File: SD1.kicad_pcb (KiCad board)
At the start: 4 copper layers, 296.7 x 122.7 mm, 246 parts, among them J101 HR861153C, J102 10118194-0001LF, J103 JST ZH 1.5mm 1x5, J104 JST 1.25mm, J107 JST 1.25mm, J301 PJ-102AH, J302 PJ-102AH, J303 Conn_01x02, J304 Conn_01x02, J402 Conn_ARM_JTAG_SWD_10, J403 FTDI_TTL_Cable, J801 Conn_01x02, J802 Conn_01x02, Q1 FDT86244, Q101 BSS138, Q102 PDTC114EU,115, Q301 DMMT5401, Q302 DMMT5401, Q801 DMMT5401, Q802 DMMT5401, SW103 Multidirection_Switch, SW401 PTS810, T1 HR051067, U102 ER-TFTM028-4, U103 CP2102N-A02-GQFN28R, U104 CC2652P, U105 W5500, U106 EKMC1691111, U107 MCP23017, U108 BME280, U109 SCD30, U2 TPS23753A, U3 TL431A, U301 110-102, U302 LMP91000, U4 TCMT1107, U501 TLV70018, U502 ADPD188BI, U503 Smoke Chamber, U601 CCS811, U701 TPS61022, U702 TLV62585, U801 MCP73831-2-OT, Y101 25MHz

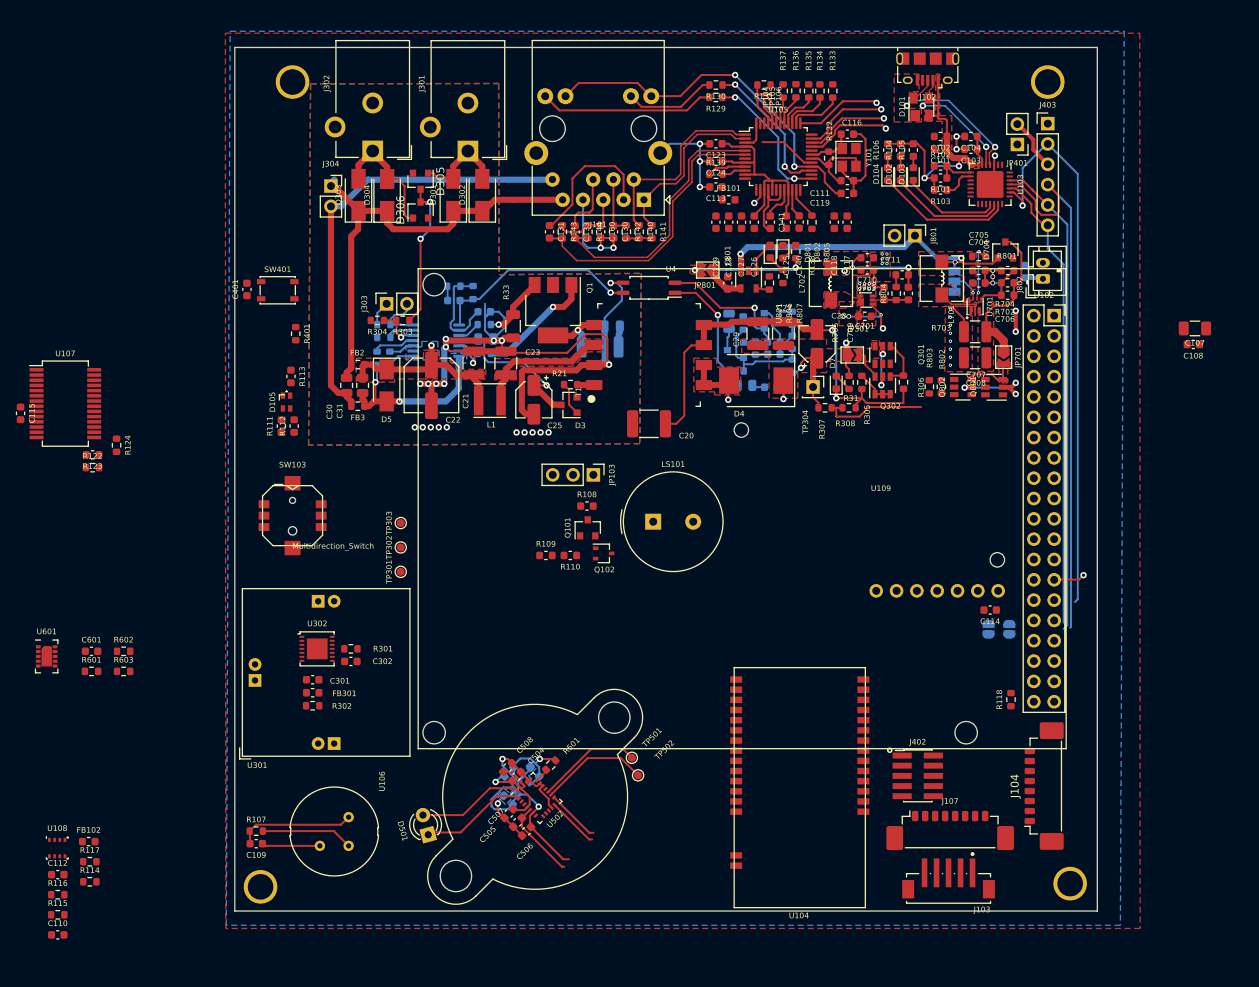
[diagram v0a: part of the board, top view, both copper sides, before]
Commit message: 4layer layout WIP, 90%.
Changed SCD30 to reverse mount. 
Connected RGB led and button to io expander.
Connected all nets to micro.
Add jumper for CTS line.
Nettie GNDA and GND for W5500 Eth.
Changed EN_5V_BST to Global.
Bugfixes net names: LCD_CS
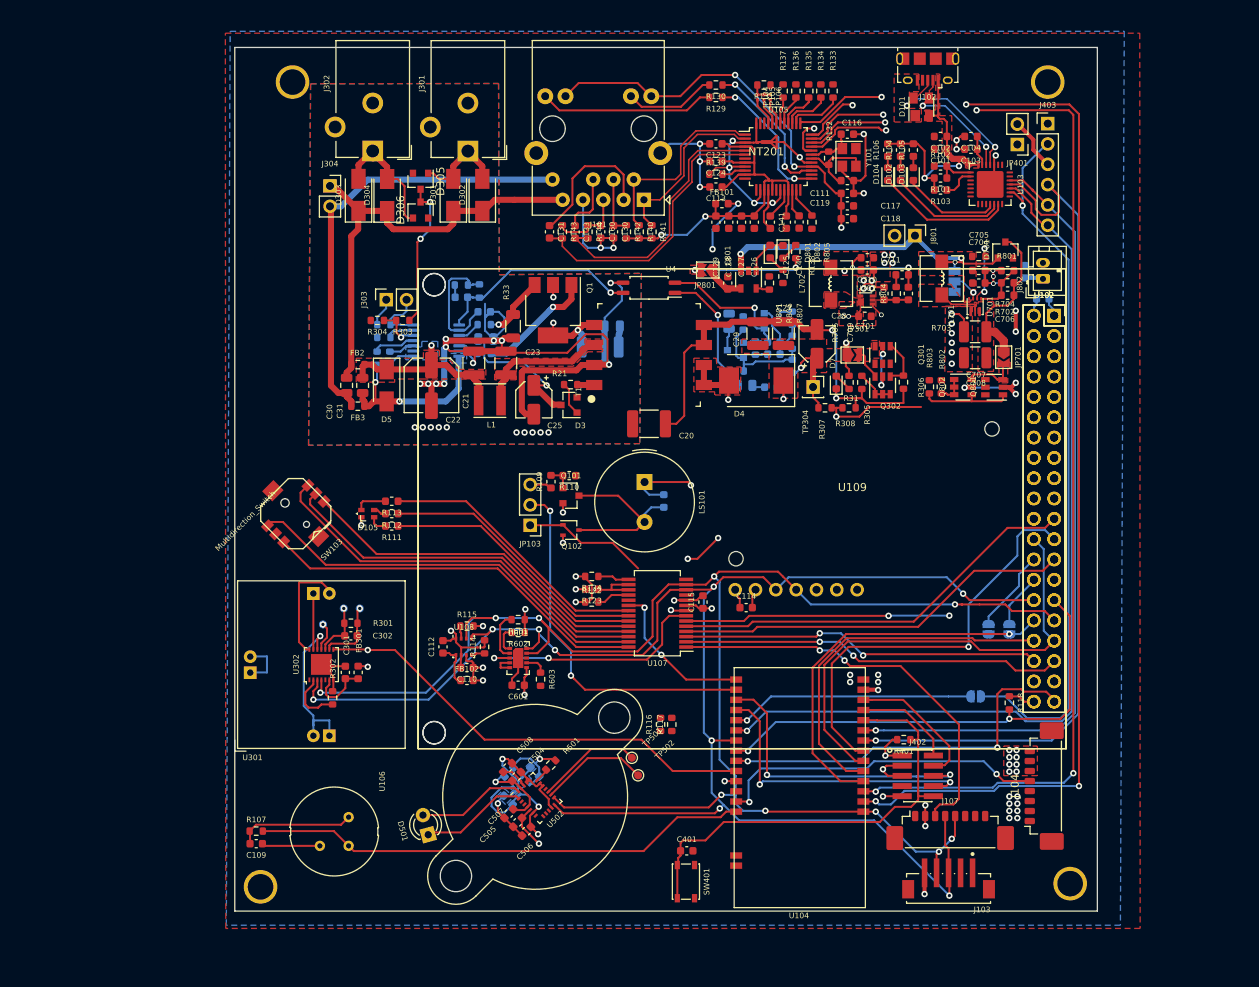
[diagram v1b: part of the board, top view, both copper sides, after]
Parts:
- removed C107: 10u, Capacitor_SMD:C_1206_3216Metric
- added JP107: Jumper_NO_Small, Jumper:SolderJumper-2_P1.3mm_Open_RoundedPad1.0x1.5mm, B.Cu at (208.2, 87.6)
- added NT201: Net-Tie_2, NetTie:NetTie-2_SMD_Pad0.5mm, F.Cu at (182.0, 18.3)
- added U102: ER-TFTM028-4, mylib:ER-TFTM028-4, F.Cu at (218.0, 40.0)
- C108, R108, TP301, TP302, TP303: moved to B.Cu
- U109: footprint mylib:SCD30 -> mylib:SCD30_reverse_mount
- moved R401 91.4 mm to (199.2, 93.0), turned to 180 degrees
- moved SW401 89.8 mm to (172.0, 110.7), turned to 270 degrees
- moved C401 89.1 mm to (172.1, 106.9), turned to 0 degrees
- moved C115 88.5 mm to (174.1, 75.8), turned to 90 degrees
- moved U107 78.5 mm to (168.4, 77.2), turned to 180 degrees
- moved R116 78.3 mm to (168.8, 91.1), turned to 90 degrees
- moved R117 74.7 mm to (170.2, 91.1), turned to 90 degrees
- moved R122 64.6 mm to (160.2, 75.8)
- moved R123 64.6 mm to (160.2, 74.2)
- moved R115 62.6 mm to (144.6, 78.8)
- moved R124 61.6 mm to (160.2, 72.6), turned to 180 degrees
- moved C110 61.1 mm to (144.6, 84.0), turned to 180 degrees
- moved U601 58.9 mm to (151.0, 82.8)
- moved R114 57.4 mm to (146.8, 81.4), turned to 90 degrees
- moved U108 56.7 mm to (144.2, 81.4)
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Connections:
- J104 pad 5: (no net) -> /RGBW_DOUT
- J402 pad 1: /TARGET_VDD -> +3V3
- J403 pad 6: /Debug and Serial/WMCU_CTS -> /WMCU_CTS
- JP103 pad 2: (no net) -> /SPKR_DRIVE
- R401 pad 2: /TARGET_VDD -> +3V3
- R801 pad 1: /Power/EN_5V_BST -> EN_5V_BST
- U102 pad 21: (no net) -> /~LCD_RESET
- U102 pad 23: (no net) -> /~LCD_CS
- U102 pad 39: (no net) -> /CTP_INT
- U103 pad 24: /Debug and Serial/WMCU_CTS -> /WMCU_CTS
- U104 pad 15: (no net) -> /IO_INT
- U104 pad 16: (no net) -> /SPKR_DRIVE
- U104 pad 2: (no net) -> /~ETH_INT
- U104 pad 20: (no net) -> /WMCU_CTS
- U104 pad 22: (no net) -> /LCD_BACKLIGHT
- U104 pad 23: (no net) -> /CTP_INT
- U104 pad 27: (no net) -> /RGBW_DOUT
- U104 pad 28: (no net) -> /PIR_SENSE
- U104 pad 3: (no net) -> /ETH_CS
- U104 pad 7: (no net) -> /~LCD_CS
- U105 pad 32: (no net) -> /ETH_CS
- U105 pad 36: (no net) -> /~ETH_INT
- U107 pad 1: /SD_CS -> /EXT_Sleep
- U107 pad 2: (no net) -> /SD_CS
- U107 pad 20: (no net) -> /IO_INT
- U107 pad 21: /I_LED_R -> /I_LED_B
- U107 pad 23: /I_LED_B -> /I_LED_R
- U107 pad 3: /LCD_DC -> /FONT_CS
- U107 pad 4: /FONT_CS -> /LCD_DC
- U107 pad 5: (no net) -> /~LCD_RESET
- U107 pad 8: /EXT_Sleep -> EN_5V_BST
- U701 pad 5: /Power/EN_5V_BST -> EN_5V_BST
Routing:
- net +3V3: track 112.9 -> 441.0 mm, vias 6 -> 23
- net I2C_SDA: track 6.78 -> 212.5 mm, vias 0 -> 10
- net I2C_SCL: track 6.49 -> 211.7 mm, vias 0 -> 9
- net +5V: track 68.0 -> 218.8 mm, vias 11 -> 20
- net /~ETH_INT: track 0.00 -> 148.9 mm, vias 0 -> 4
- net /ETH_CS: track 0.00 -> 148.7 mm, vias 0 -> 4
- net /WMCU_CTS: track 0.00 -> 113.3 mm, vias 0 -> 1
- net EN_5V_BST: track 0.00 -> 94.7 mm, vias 0 -> 3
- net 5V_MainDet: track 13.6 -> 79.0 mm, vias 0 -> 4
- net /LCD_BACKLIGHT: track 0.00 -> 59.6 mm, vias 0 -> 2
- net SPI_SCK: track 91.1 -> 150.1 mm
- net /WMCU_RESET: track 0.00 -> 58.6 mm
- net /Debug and Serial/WMCU_CTS: track 57.8 -> 0.00 mm
- net /CO_ADC: track 0.00 -> 56.6 mm, vias 0 -> 1
- net SPI_MOSI: track 98.7 -> 153.1 mm, vias 2 -> 1
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- added copper zone on F.Cu, net +5V
- added copper zone on F.Cu, net /Debug and Serial/5V_USB
- added copper zone on In2.Cu, net GND
- removed copper zone on F.Cu, net /5V_USB
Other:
- net class Default: clearance 0.2 -> 0.1524
- rule trace_clearance: 0.2 -> 0.1524

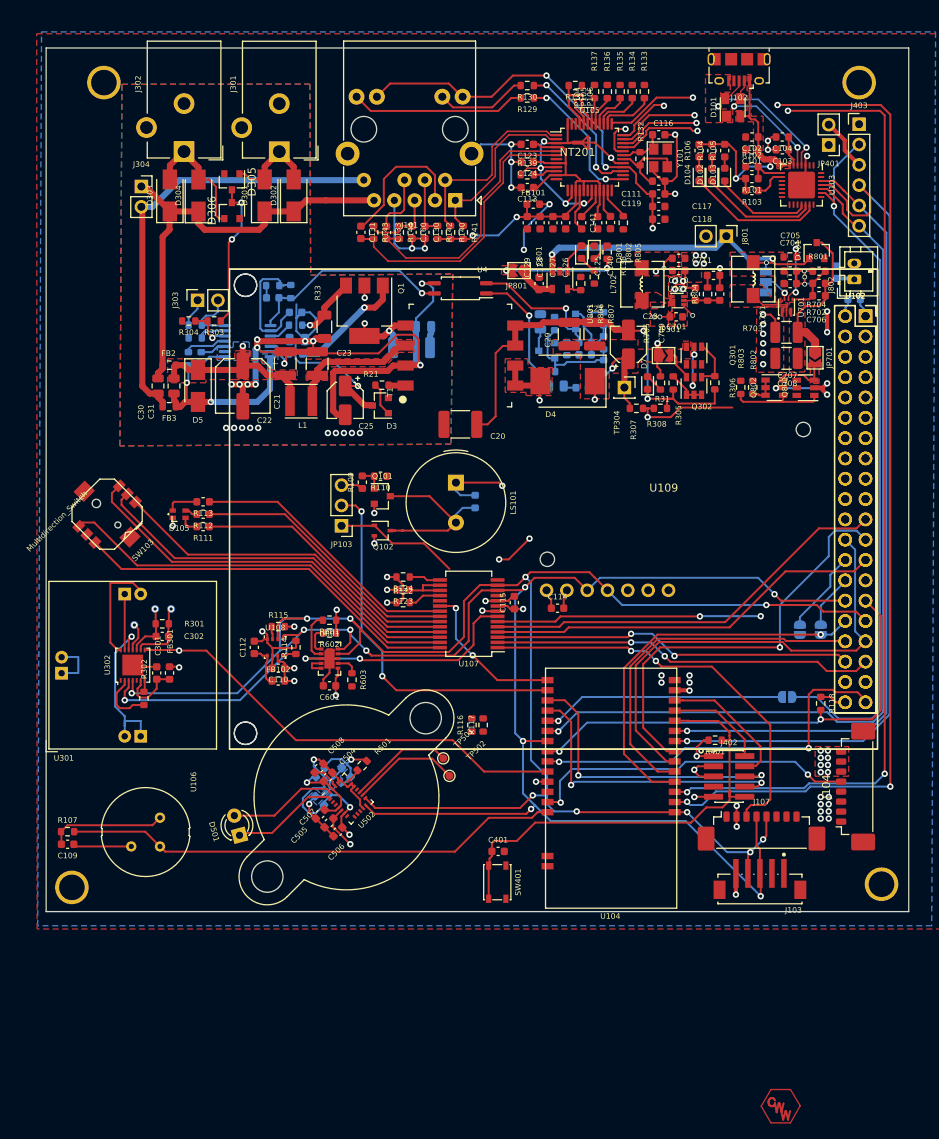
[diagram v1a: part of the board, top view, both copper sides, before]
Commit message: Layout WIP, sch final
USB 5V Jumper works for both FTDI and microusb
Added decoupling caps for micro
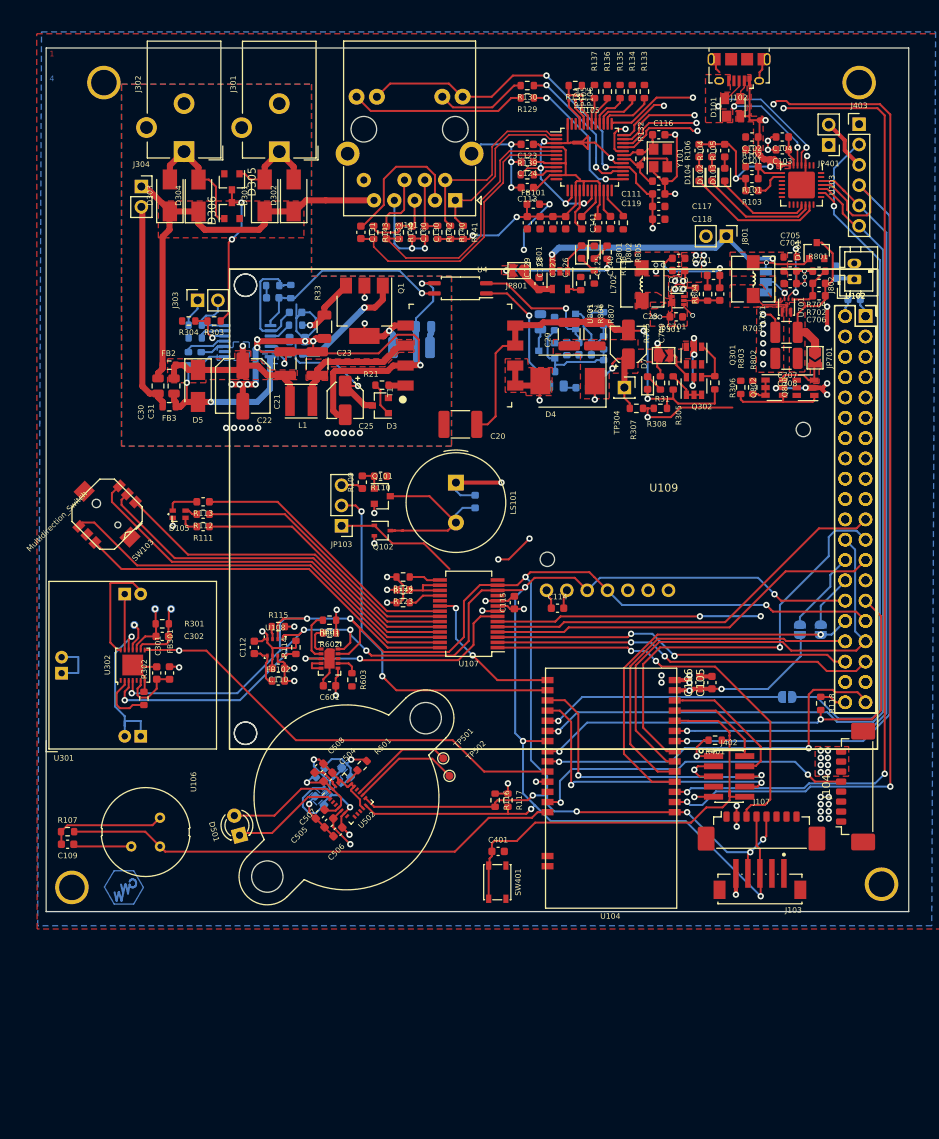
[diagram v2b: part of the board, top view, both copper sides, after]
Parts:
- added C105: 10u, Capacitor_SMD:C_0603_1608Metric, F.Cu at (198.8, 85.8)
- added C106: 1u, Capacitor_SMD:C_0603_1608Metric, F.Cu at (197.3, 85.8)
- LOGO101: moved to B.Cu
- moved LOGO101 86.5 mm to (125.3, 111.5), turned to 180 degrees
- moved R117 9.90 mm to (173.3, 100.5), turned to 270 degrees
- moved R116 9.84 mm to (171.7, 100.5), turned to 270 degrees
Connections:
- J403 pad 3: Net-(J403-Pad3) -> /Debug and Serial/5V_USB
- JP401 pad 2: Net-(J403-Pad3) -> /Debug and Serial/5V_USB
- U102 pad 10: (no net) -> Net-(U102-Pad10) (x2)
- U102 pad 11: (no net) -> Net-(U102-Pad11) (x2)
- U102 pad 12: (no net) -> Net-(U102-Pad12) (x2)
- U102 pad 13: (no net) -> Net-(U102-Pad13) (x2)
- U102 pad 14: (no net) -> Net-(U102-Pad14) (x2)
- U102 pad 15: (no net) -> Net-(U102-Pad15) (x2)
- U102 pad 16: (no net) -> Net-(U102-Pad16) (x2)
- U102 pad 17: (no net) -> Net-(U102-Pad17) (x2)
- U102 pad 18: (no net) -> Net-(U102-Pad18) (x2)
- U102 pad 19: (no net) -> Net-(U102-Pad19) (x2)
- U102 pad 20: (no net) -> Net-(U102-Pad20) (x2)
- U102 pad 22: (no net) -> Net-(U102-Pad22) (x2)
- U102 pad 3: (no net) -> Net-(U102-Pad3) (x2)
- U102 pad 37: (no net) -> Net-(U102-Pad37) (x2)
- U102 pad 38: (no net) -> Net-(U102-Pad38) (x2)
- U102 pad 4: (no net) -> Net-(U102-Pad4) (x2)
- U102 pad 5: (no net) -> Net-(U102-Pad5) (x2)
- U102 pad 6: (no net) -> Net-(U102-Pad6) (x2)
- U102 pad 7: (no net) -> Net-(U102-Pad7) (x2)
- U102 pad 8: (no net) -> Net-(U102-Pad8) (x2)
- U102 pad 9: (no net) -> Net-(U102-Pad9) (x2)
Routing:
- net +5V: track 218.8 -> 277.3 mm, vias 20 -> 22
- net +3V3: track 441.0 -> 470.1 mm, vias 23 -> 26
- net /Debug and Serial/5V_USB: track 32.0 -> 48.4 mm, vias 2 -> 3
- net GND: track 216.0 -> 225.7 mm
- net Net-(J403-Pad3): track 6.65 -> 0.00 mm
- net 5V_Main: track 58.8 -> 57.8 mm
- net I2C_SCL: track 211.7 -> 212.6 mm
- net 5V_MainDet: track 79.0 -> 78.5 mm
- added copper zone on In1.Cu, net +3V3
- added copper zone on F.Cu, net /Eth + PoE/PoE Flyback/VP
- added copper zone on In1.Cu, net GNDD
- removed copper zone on F.Cu, net (none)
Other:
- board text added: "1"
- board text added: "2"
- board text added: "3"
- board text added: "4"
- board text added: "SAEMS r0, 12/12/20 Daniel Mulvaney Clayton White"

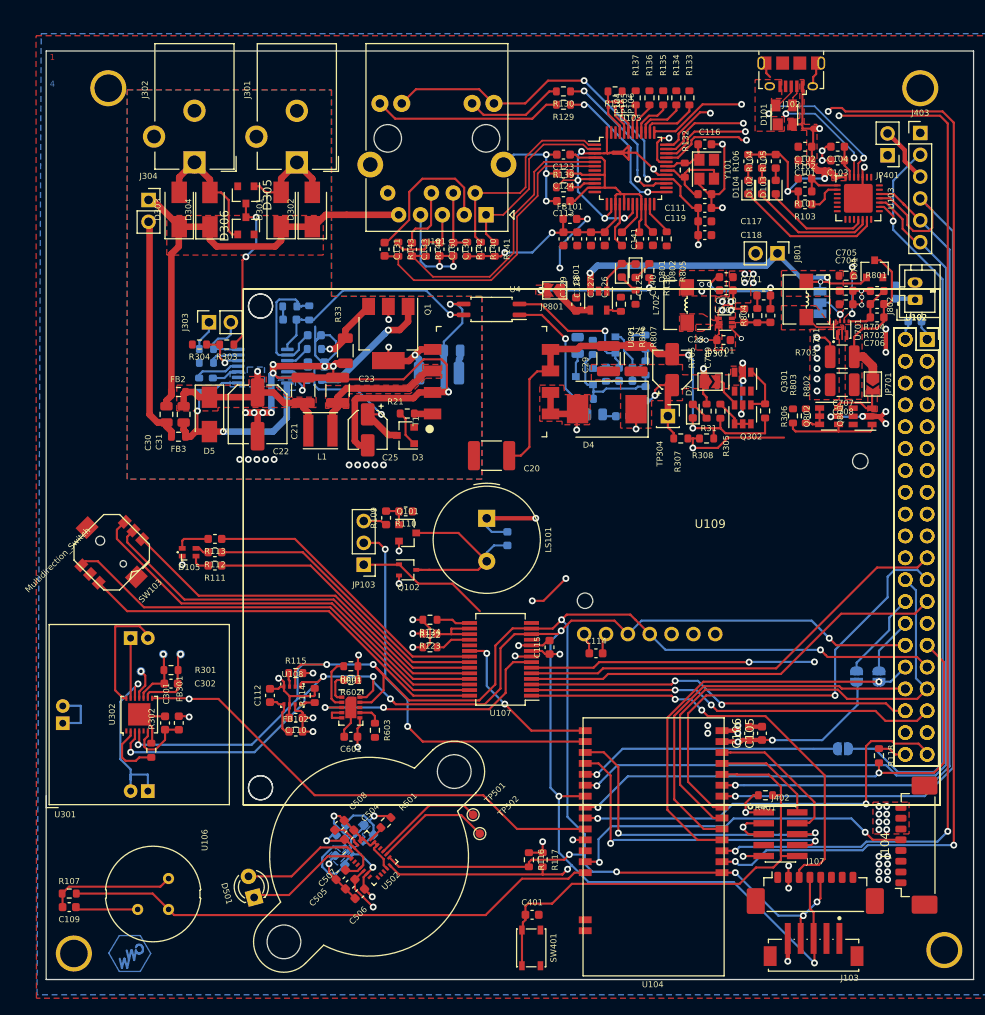
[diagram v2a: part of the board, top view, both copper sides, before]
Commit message: Re-annotate all parts
Cleans up annotations
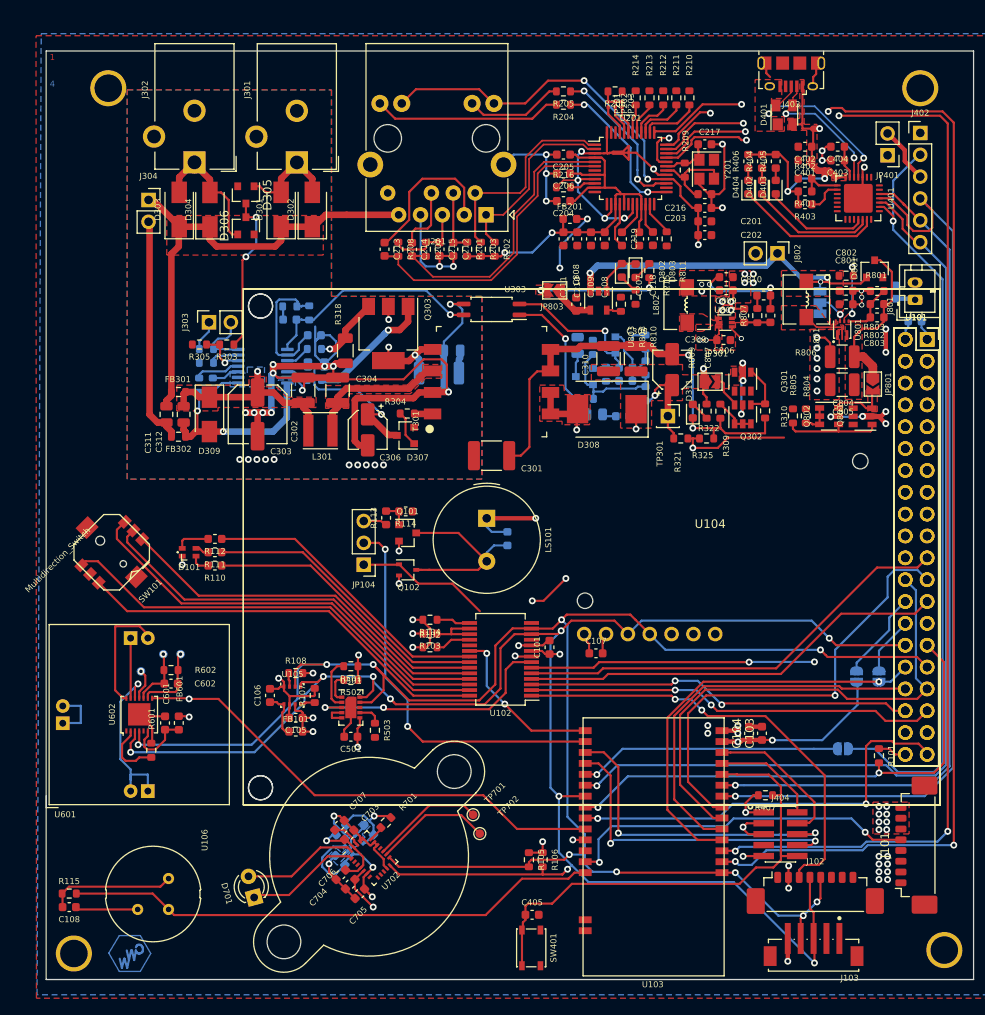
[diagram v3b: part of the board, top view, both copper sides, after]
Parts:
- renumbered C115 to C101, C108 to C102, C105 to C103, C106 to C104, C110 to C105, C112 to C106, C114 to C107, C109 to C108, C117 to C201, C118 to C202, C119 to C203, C113 to C204, C123 to C205, C124 to C206, C125 to C207, C126 to C208, C127 to C209, C128 to C210, C129 to C211, C130 to C212, C131 to C213, C133 to C214, C160 to C215, C111 to C216, C116 to C217, C140 to C218, C141 to C219, C20 to C301, C21 to C302, C22 to C303, C23 to C304, C24 to C305, C25 to C306, C26 to C307, C27 to C308, C28 to C309, C29 to C310, C30 to C311, C31 to C312, C32 to C313, C33 to C314, C34 to C315, C35 to C316, C36 to C317, C37 to C318, C101 to C401, C102 to C402, C103 to C403, C104 to C404, C401 to C405, C601 to C501, C301 to C601, C302 to C602, C501 to C701, C502 to C702, C504 to C703, C505 to C704, C506 to C705, C507 to C706, C508 to C707, C704 to C801, C705 to C802, C706 to C803, C707 to C804, C708 to C805, C701 to C806, C709 to C807, C801 to C808, C710 to C809, C711 to C810, C802 to C811, D105 to D101, D3 to D307, D4 to D308, D5 to D309, D6 to D310, D7 to D311, D101 to D401, D102 to D402, D103 to D403, D104 to D404, D501 to D701, D701 to D801, D801 to D802, D802 to D803, FB102 to FB101, FB101 to FB201, FB2 to FB301, FB3 to FB302, FB301 to FB601, FB501 to FB701, J104 to J101, J107 to J102, J101 to J201, J403 to J402, J102 to J403, J402 to J404, J802 to J801, J801 to J802, JP107 to JP103, JP103 to JP104, JP104 to JP201, JP105 to JP202, JP106 to JP203, JP701 to JP801, JP702 to JP802, JP801 to JP803, L1 to L301, L701 to L801, L702 to L802, Q1 to Q303, R118 to R101, R122 to R102, R123 to R103, R124 to R104, R116 to R105, R117 to R106, R114 to R107, R115 to R108, R108 to R109, R111 to R110, R112 to R111, R113 to R112, R109 to R113, R110 to R114, R107 to R115, R142 to R201, R141 to R202, R140 to R203, R129 to R204, R130 to R205, R131 to R206, R144 to R207, R143 to R208, R132 to R209, R133 to R210, R134 to R211, R135 to R212, R136 to R213, R137 to R214, R138 to R215, R139 to R216, R19 to R301, R20 to R302, R21 to R304, R304 to R305, R22 to R306, R23 to R307, R24 to R308, R305 to R309, R306 to R310, R25 to R311, R26 to R312, R27 to R313, R28 to R314, R29 to R315, R30 to R316, R32 to R317, R33 to R318, R34 to R319, R35 to R320, R307 to R321, R31 to R322, R36 to R323, R37 to R324, R308 to R325, R101 to R401, R102 to R402, R103 to R403, R104 to R404, R105 to R405, R106 to R406, R401 to R407, R601 to R501, R602 to R502, R603 to R503, R302 to R601, R301 to R602, R501 to R701, R702 to R802, R704 to R803, R802 to R804, R803 to R805, R703 to R806, R804 to R807, R806 to R808, R705 to R809, R807 to R810, R805 to R811, SW103 to SW101, T1 to T301, TP304 to TP301, TP301 to TP601, TP302 to TP602, TP303 to TP603, TP501 to TP701, TP502 to TP702, U102 to U101, U107 to U102, U104 to U103, U109 to U104, U108 to U105, U105 to U201, U2 to U301, U3 to U302, U4 to U303, U103 to U401, U601 to U501, U301 to U601, U302 to U602, U501 to U701, U502 to U702, U503 to U703, U701 to U801, U702 to U802, U801 to U803, Y101 to Y201
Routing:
- added copper zone on F.Cu, net Net-(JP701-Pad2)

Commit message: Prefinal, layout done
Update FB to use inductor footprints
DNP net tie
Update diode symbol in power
Add battery voltage divider in power
Supply 5V power to aux sensor connector
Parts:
- removed the U101 at (218.0, 40.0)
- added R812: 10k, Resistor_SMD:R_0603_1608Metric, B.Cu at (202.7, 32.7)
- added R813: 10k, Resistor_SMD:R_0603_1608Metric, B.Cu at (199.7, 32.7)
- FB301, FB302: footprint Resistor_SMD:R_0603_1608Metric -> Inductor_SMD:L_0603_1608Metric
- moved J802 0.60 mm to (200.6, 29.4)
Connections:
- J102 pad 1: (no net) -> +5V
- U101 pad 10: Net-(U101-Pad10) -> (no net)
- U101 pad 11: Net-(U101-Pad11) -> (no net)
- U101 pad 12: Net-(U101-Pad12) -> (no net)
- U101 pad 13: Net-(U101-Pad13) -> (no net)
- U101 pad 14: Net-(U101-Pad14) -> (no net)
- U101 pad 15: Net-(U101-Pad15) -> (no net)
- U101 pad 16: Net-(U101-Pad16) -> (no net)
- U101 pad 17: Net-(U101-Pad17) -> (no net)
- U101 pad 18: Net-(U101-Pad18) -> (no net)
- U101 pad 19: Net-(U101-Pad19) -> (no net)
- U101 pad 20: Net-(U101-Pad20) -> (no net)
- U101 pad 22: Net-(U101-Pad22) -> (no net)
- U101 pad 3: Net-(U101-Pad3) -> (no net)
- U101 pad 37: Net-(U101-Pad37) -> (no net)
- U101 pad 38: Net-(U101-Pad38) -> (no net)
- U101 pad 4: Net-(U101-Pad4) -> (no net)
- U101 pad 5: Net-(U101-Pad5) -> (no net)
- U101 pad 6: Net-(U101-Pad6) -> (no net)
- U101 pad 7: Net-(U101-Pad7) -> (no net)
- U101 pad 8: Net-(U101-Pad8) -> (no net)
- U101 pad 9: Net-(U101-Pad9) -> (no net)
- U103 pad 26: (no net) -> BATT_Det
- U701 pad 4: (no net) -> GND
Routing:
- net BATT_Det: track 0.00 -> 106.5 mm, vias 0 -> 2
- net +5V: track 277.3 -> 262.6 mm, vias 22 -> 25
- net /SPKR_Alt: track 15.6 -> 3.90 mm
- net 5V_MainDet: track 78.5 -> 67.3 mm
- net GND: track 225.7 -> 233.3 mm, vias 53 -> 57
- net +3V3: track 470.1 -> 463.4 mm
- net +BATT: track 54.7 -> 57.3 mm
- net I2C_SDA: track 212.6 -> 210.7 mm
- net /IO_INT: track 19.5 -> 20.9 mm
- net /Eth + PoE/PoE Flyback/DC_BARREL: track 16.6 -> 15.9 mm
- net I2C_SCL: track 212.6 -> 212.0 mm
- removed copper zone on F.Cu, net Net-(JP701-Pad2)
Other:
- board size 296.7 x 122.7 mm -> 107.8 x 108 mm
